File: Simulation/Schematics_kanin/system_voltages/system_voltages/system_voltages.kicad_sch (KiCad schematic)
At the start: 17 parts

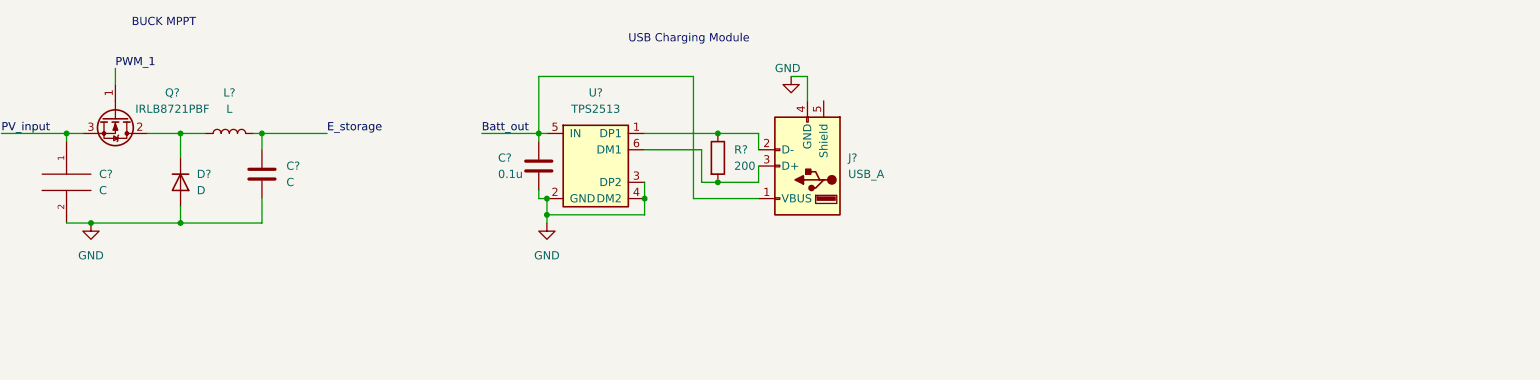
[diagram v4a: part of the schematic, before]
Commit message: Added 5V/2A LDO
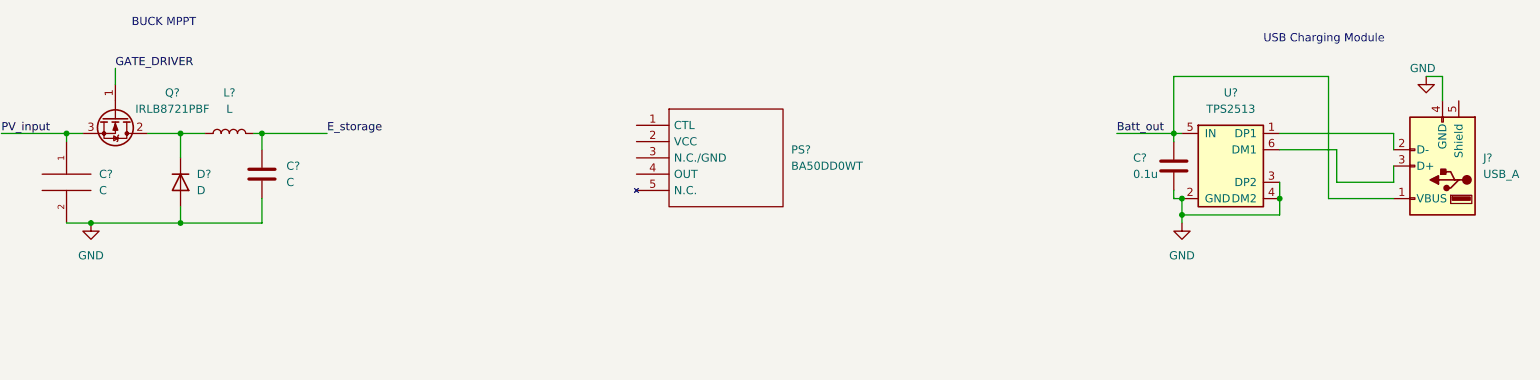
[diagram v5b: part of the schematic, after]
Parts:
- removed R?: 200, symbol Device:R
- added PS?: BA50DD0WT, TO178P480X1010X1810-5P, symbol SamacSys_Parts:BA50DD0WT
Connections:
- net PWM_1 renamed GATE_DRIVER
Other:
- moved on the sheet: C?, J?, U?

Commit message: Pushing everything for Lukas
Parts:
- removed D?: D, symbol Device:D
- added Q?: IRLB8721PBF, Package_TO_SOT_THT:TO-220-3_Vertical, symbol Transistor_FET:IRLB8721PBF
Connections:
- net Batt_out: now also PS?.4 (OUT)
- net E_storage: now also PS?.2 (VCC)
- net GND: now also PS?.3 (N.C./GND), Q?.3 (S)
- net PV_input: now also Q?.2 (D); no longer Q?.3 (S)
- net MCU_5v: now reaches PS?.1 (CTL)
- net at L?.1: now also Q?.3 (S), Q?.2 (D); no longer Q?.2 (D)
- new net GATE_DRIVER2: Q?.1 (G)
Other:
- note added: "5V/2A to USB Charging"
- moved on the sheet: C1, C2, C3, D1, D2, PS?, Q?, R1, R2, U?

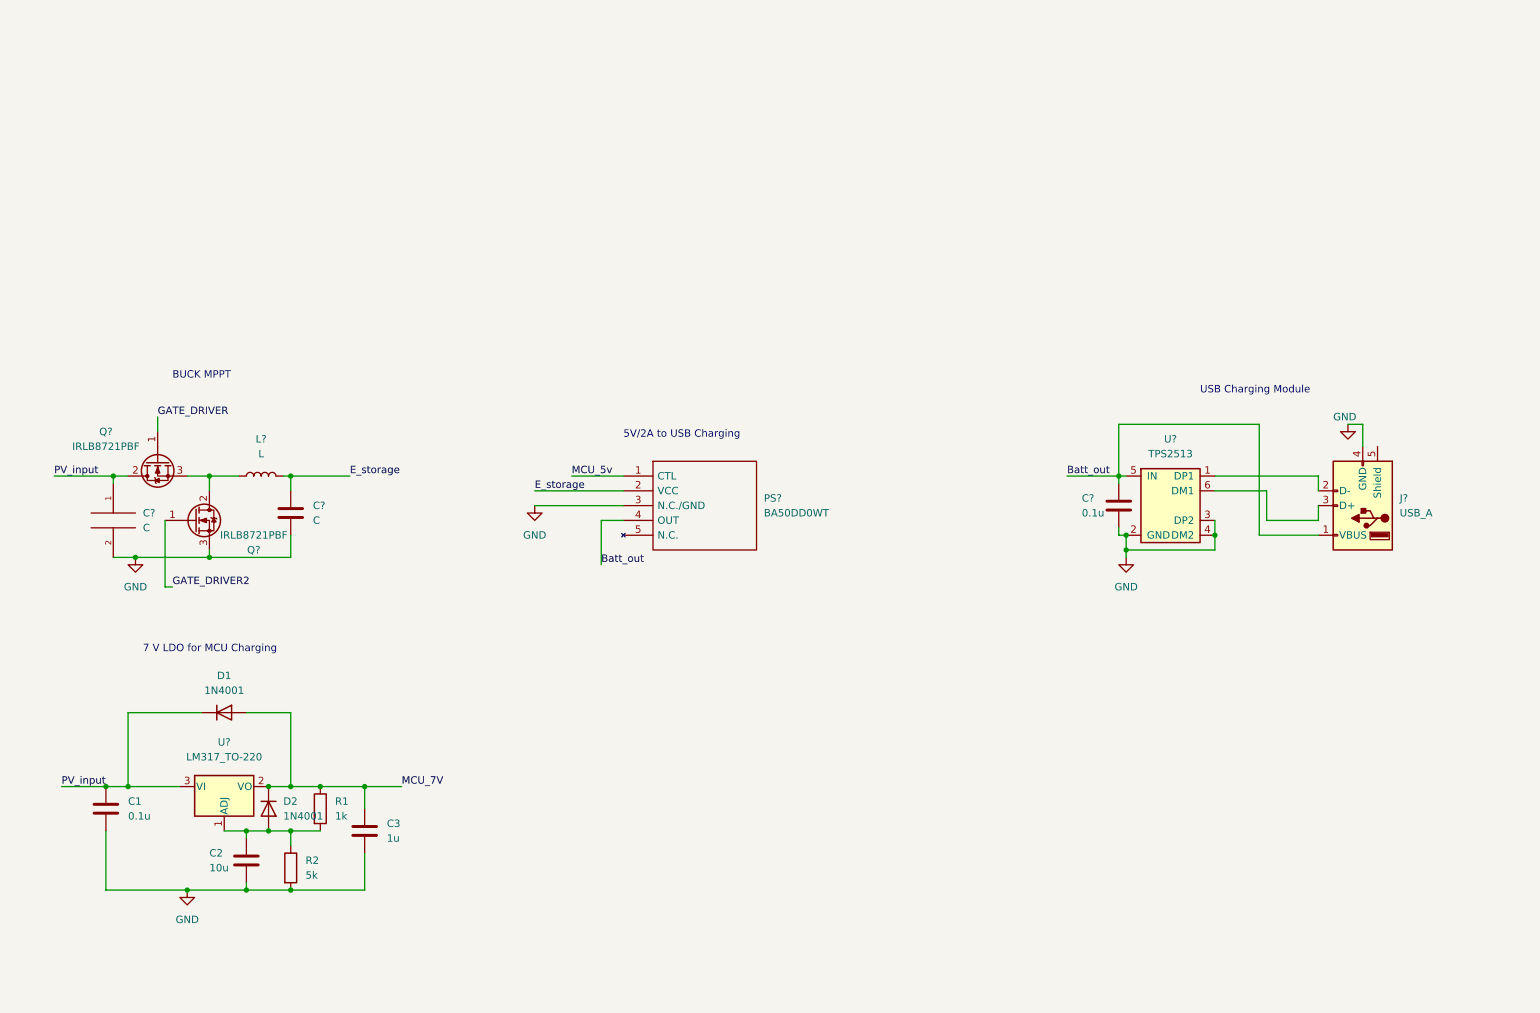
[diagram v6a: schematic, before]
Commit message: Adding changes to gate driver ckt
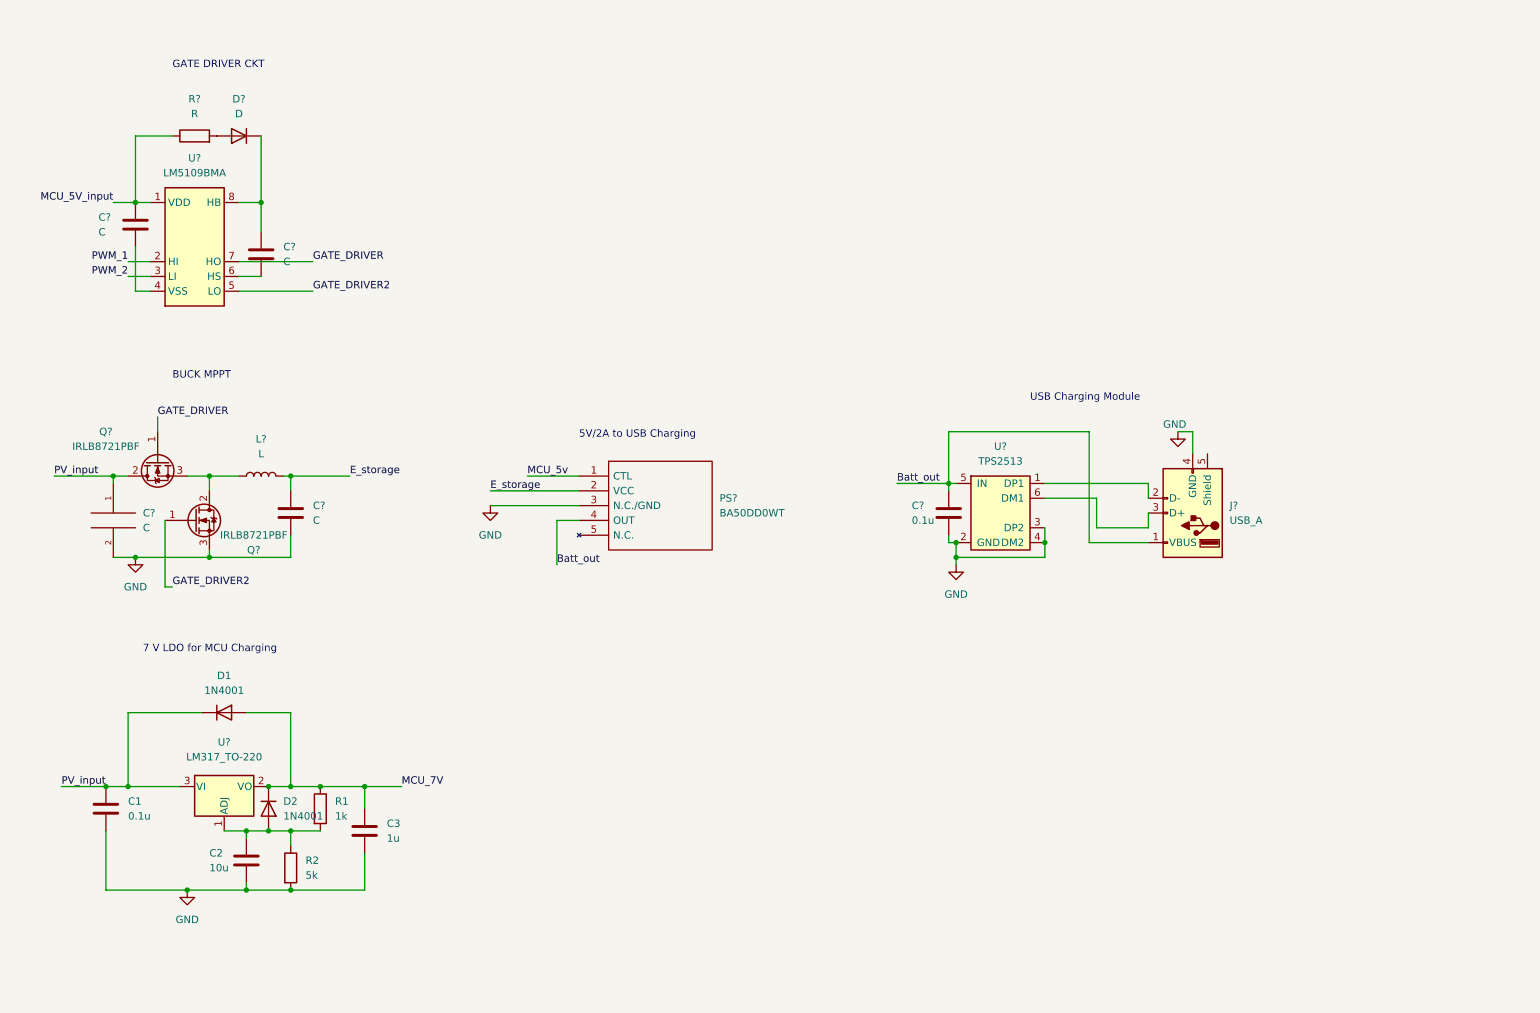
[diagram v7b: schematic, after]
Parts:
- added C? (x2): C, symbol Device:C
- added D?: D, symbol Device:D
- added R?: R, symbol Device:R
- added U?: LM5109BMA, Package_SO:SOIC-8_3.9x4.9mm_P1.27mm, symbol Driver_FET:LM5109BMA
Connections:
- net GATE_DRIVER: now also U?.7 (HO)
- net GATE_DRIVER2: now also U?.5 (LO)
- new net: D?.2 (A), R?.2
- new net: C?.1, D?.1 (K), U?.8 (HB)
- new net: C?.2, U?.6 (HS)
- new net: C?.2, U?.4 (VSS)
- new net MCU_5V_input: C?.1, R?.1, U?.1 (VDD)
- new net PWM_1: U?.2 (HI)
- new net PWM_2: U?.3 (LI)
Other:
- note added: "GATE DRIVER CKT"
- moved on the sheet: C?, J?, PS?, U?

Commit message: Started routing our footprints
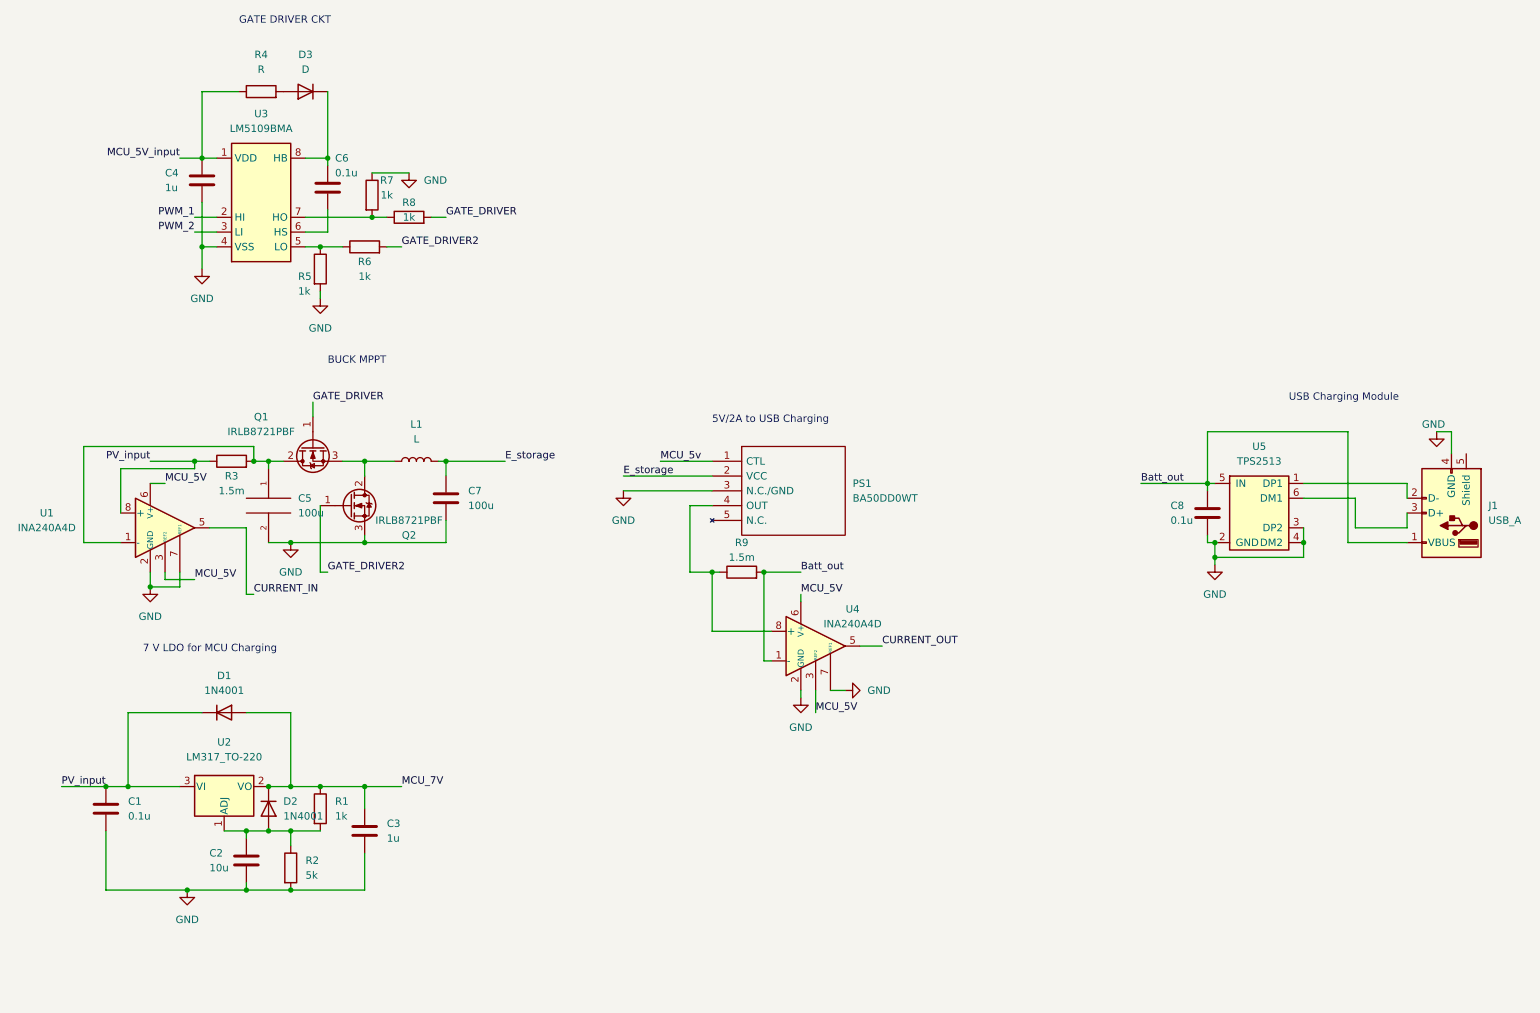
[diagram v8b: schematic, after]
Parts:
- added R3, R9: 1.5m, Resistor_SMD:R_0805_2012Metric_Pad1.20x1.40mm_HandSolder, symbol Device:R
- added R5, R6, R7, R8: 1k, Resistor_SMD:R_0805_2012Metric_Pad1.20x1.40mm_HandSolder, symbol Device:R
- added U1, U4: INA240A4D, Package_SO:SOIC-8_3.9x4.9mm_P1.27mm, symbol Amplifier_Current:INA240A4D
- C1, C2, C3: footprint (none) -> Capacitor_SMD:C_0805_2012Metric_Pad1.18x1.45mm_HandSolder
- C4: renamed from C?; value C -> 1u; footprint (none) -> Capacitor_SMD:C_0805_2012Metric_Pad1.18x1.45mm_HandSolder
- C5, C7: renamed from C?; value C -> 100u; footprint (none) -> Capacitor_SMD:C_0805_2012Metric_Pad1.18x1.45mm_HandSolder
- C6: renamed from C?; value C -> 0.1u; footprint (none) -> Capacitor_SMD:C_0805_2012Metric_Pad1.18x1.45mm_HandSolder
- C8: renamed from C?; footprint (none) -> Capacitor_SMD:C_0805_2012Metric_Pad1.18x1.45mm_HandSolder
- R1, R2: footprint (none) -> Resistor_SMD:R_0805_2012Metric_Pad1.20x1.40mm_HandSolder
- R4: renamed from R?; footprint (none) -> Resistor_SMD:R_0805_2012Metric_Pad1.20x1.40mm_HandSolder
- gave numbers to parts that had none: 9
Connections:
- net Batt_out: now also R9.2, U4.1 (-); no longer PS1.4 (OUT)
- net GATE_DRIVER: now also R8.2; no longer U3.7 (HO)
- net GATE_DRIVER2: now also R6.2; no longer U3.5 (LO)
- net GND: now also C4.2, U3.4 (VSS), R5.2, R7.1, U1.2 (GND), U1.4 (GND), U1.7 (REF1), U4.2 (GND), U4.4 (GND), U4.7 (REF1)
- net PV_input: now also R3.1, U1.8 (+); no longer C5.1, Q1.2 (D)
- new net: PS1.4 (OUT), R9.1, U4.8 (+)
- new net: R5.1, R6.1, U3.5 (LO)
- new net: R7.2, R8.1, U3.7 (HO)
- new net: C5.1, Q1.2 (D), R3.2, U1.1 (-)
- new net CURRENT_IN: U1.5
- new net CURRENT_OUT: U4.5
- new net MCU_5V: U1.3 (REF2), U1.6 (V+), U4.3 (REF2), U4.6 (V+)
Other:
- moved on the sheet: C4, C5, C6, C7, C8, D3, J1, L1, PS1, Q1, Q2, R4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
